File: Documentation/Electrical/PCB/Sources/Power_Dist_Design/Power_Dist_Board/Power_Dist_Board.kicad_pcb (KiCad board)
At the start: 2 copper layers, 145 x 85 mm, 66 parts, among them J1 Battery Connector, J10 GND_Bridge_3, J2 +5V, J3 +5V, J4 +3.3V, J5 +3.3V, J6 GND, J7 GND, J8 GND_Bridge_1, J9 GND_Bridge_2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

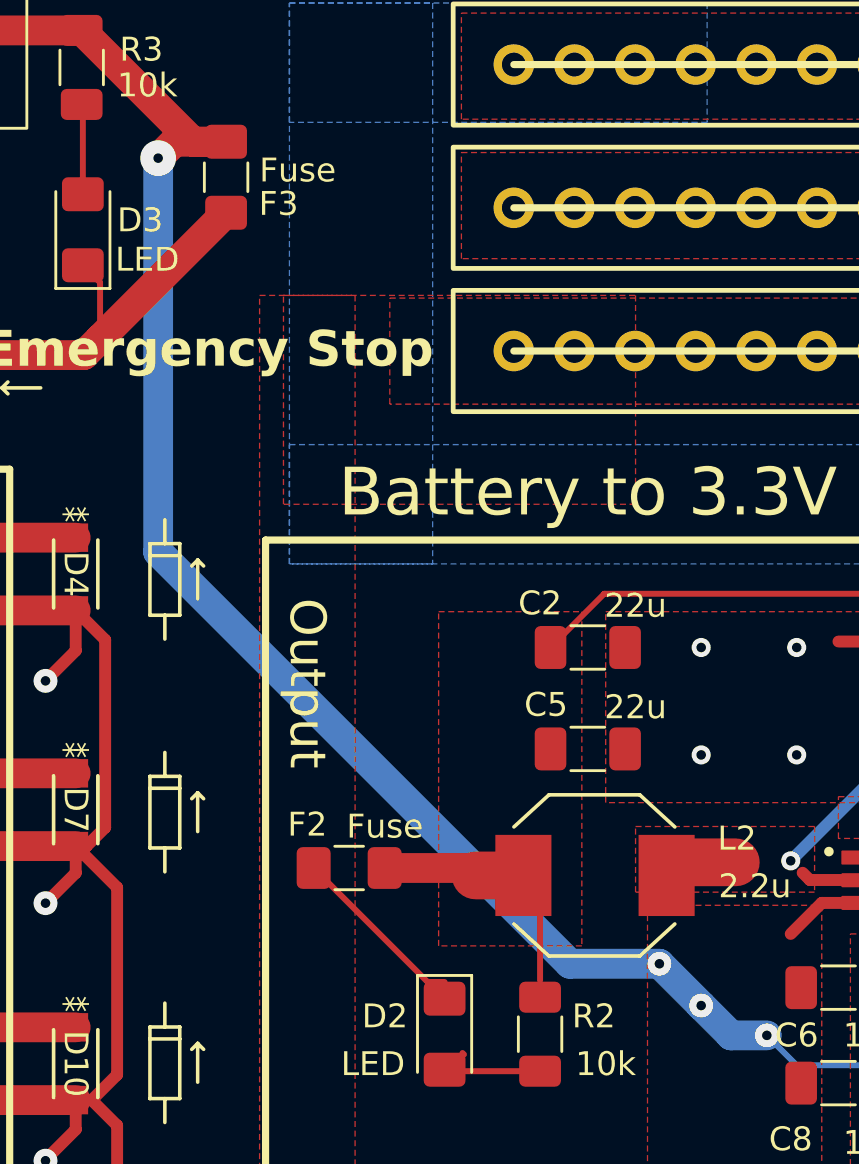
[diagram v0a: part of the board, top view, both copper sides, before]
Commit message: Added keepout zones under inductors that were accidentally removed at some point
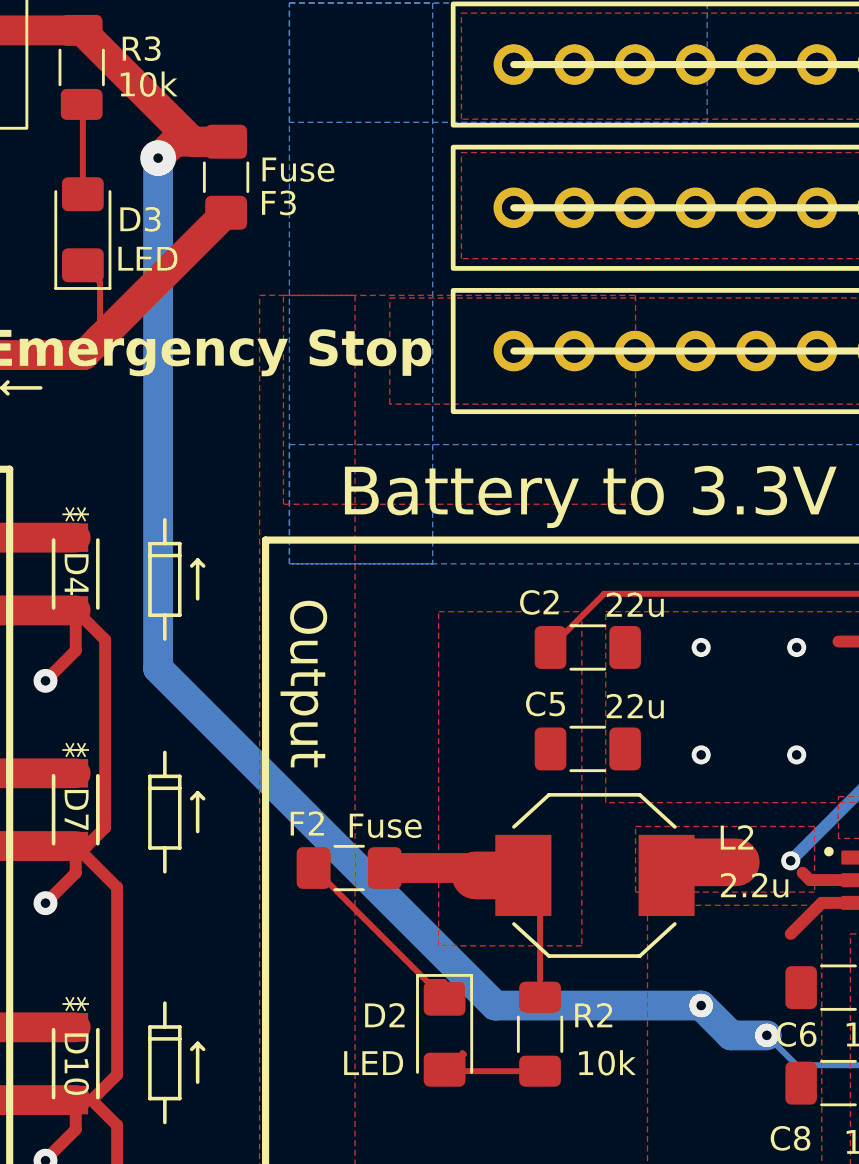
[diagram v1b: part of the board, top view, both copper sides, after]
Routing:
- net /vin: track 109.5 -> 112.4 mm, vias 7 -> 6
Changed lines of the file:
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@@
   (via (at 197.0625 70.5) (size 0.8) (drill 0.4) (layers "F.Cu" "B.Cu") (net 4))
   (via (at 132 69.75) (size 1) (drill 0.4) (layers "F.Cu" "B.Cu") (net 4))
-  (via (at 127.5 66.75) (size 1) (drill 0.4) (layers "F.Cu" "B.Cu") (net 4))
   (via (at 148.5 71) (size 0.8) (drill 0.4) (layers "F.Cu" "B.Cu") (net 4))
+  (segment (start 106.5 54.383884) (end 106.5 33) (width 1.25) (layer "B.Cu") (net 4))
   (segment (start 181.5625 70.5) (end 180.5625 69.5) (width 0.25) (layer "B.Cu") (net 4))
-  (segment (start 106.5 49.5) (end 106.5 33) (width 1.25) (layer "B.Cu") (net 4))
-  (segment (start 123.75 66.75) (end 127.5 66.75) (width 1.25) (layer "B.Cu") (net 4))
-  (segment (start 123.75 66.75) (end 106.5 49.5) (width 1.25) (layer "B.Cu") (net 4))
   (segment (start 148.5 71) (end 133.25 71) (width 0.25) (layer "B.Cu") (net 4))
+  (segment (start 129.25 68.5) (end 120.616116 68.5) (width 1.25) (layer "B.Cu") (net 4))
   (segment (start 197.0625 70.5) (end 181.5625 70.5) (width 0.25) (layer "B.Cu") (net 4))
   (segment (start 129.25 68.5) (end 130.5 69.75) (width 1.25) (layer "B.Cu") (net 4))
-  (segment (start 127.5 66.75) (end 129.25 68.5) (width 1.25) (layer "B.Cu") (net 4))
   (segment (start 133.25 71) (end 132 69.75) (width 0.25) (layer "B.Cu") (net 4))
   (segment (start 130.5 69.75) (end 132 69.75) (width 1.25) (layer "B.Cu") (net 4))
+  (segment (start 120.616116 68.5) (end 106.5 54.383884) (width 1.25) (layer "B.Cu") (net 4))
   (segment (start 177.399999 62.5) (end 178.1 62.5) (width 2) (layer "F.Cu") (net 5))
   (segment (start 188 60) (end 188 58.0625) (width 0.5) (layer "F.Cu") (net 5))
@@
       )
     )
+  )
+  (zone (net 0) (net_name "") (layer "B.Cu") (hatch edge 0.5)
+    (connect_pads (clearance 0))
+    (min_thickness 0.25) (filled_areas_thickness no)
+    (keepout (tracks not_allowed) (vias not_allowed) (pads not_allowed) (copperpour not_allowed) (footprints allowed))
+    (fill (thermal_gap 0.5) (thermal_bridge_width 0.5))
+    (polygon
+      (pts
+        (xy 119.75 59)
+        (xy 129.75 59)
+        (xy 129.75 67)
+        (xy 119.75 67)
+      )
+    )
+  )
+  (zone (net 0) (net_name "") (layer "B.Cu") (hatch edge 0.5)
+    (connect_pads (clearance 0))
+    (min_thickness 0.25) (filled_areas_thickness no)
+    (keepout (tracks not_allowed) (vias not_allowed) (pads not_allowed) (copperpour not_allowed) (footprints allowed))
+    (fill (thermal_gap 0.5) (thermal_bridge_width 0.5))
+    (polygon
+      (pts
+        (xy 168.5 59)
+        (xy 178.5 59)
+        (xy 178.5 67)
+        (xy 168.5 67)
+      )
+    )
